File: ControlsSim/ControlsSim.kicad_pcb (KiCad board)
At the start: 2 copper layers, 100 x 100 mm, 25 parts, among them J2 Accelerator Pot, J3 Brake Button, J5 Motor Contactors, J6 Array Contactors, J7 Rotary Switch, SW2 SW_Rotary2x6

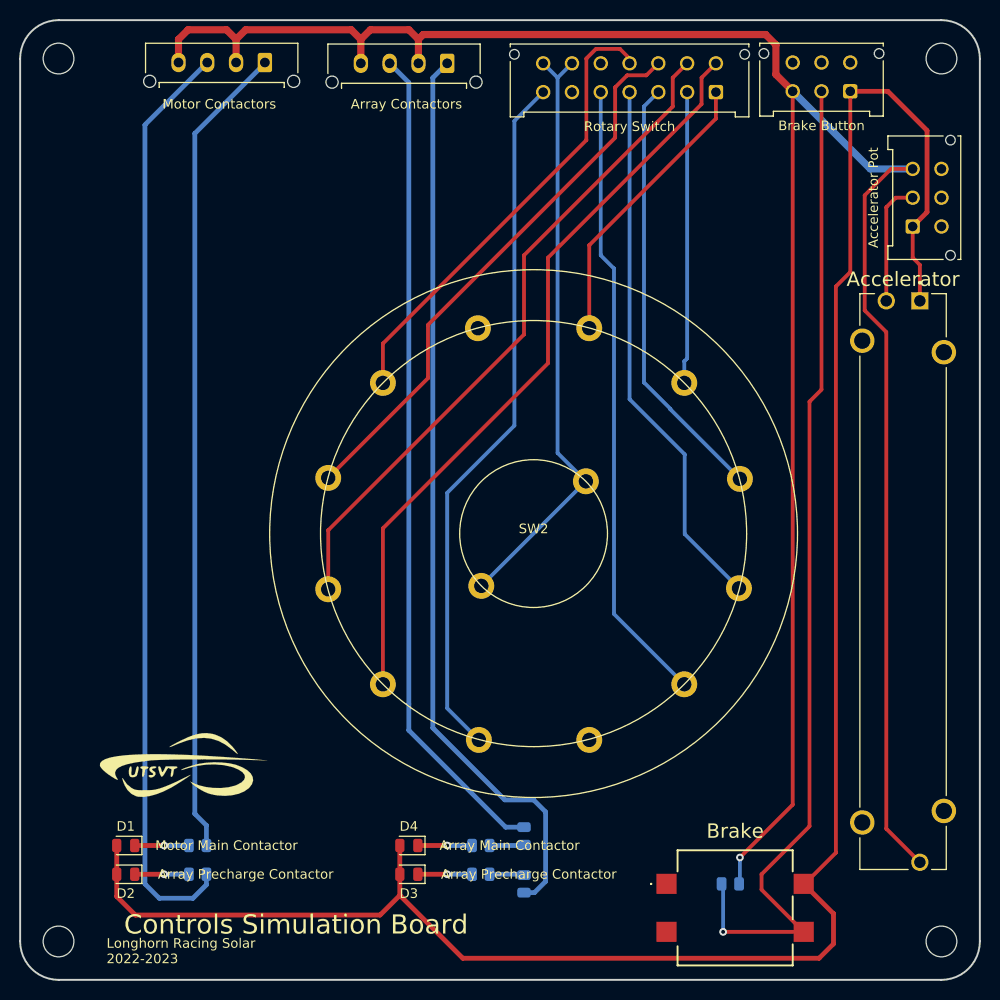
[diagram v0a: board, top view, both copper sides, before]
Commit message: shortened traces of contactor LEDs, moved upward
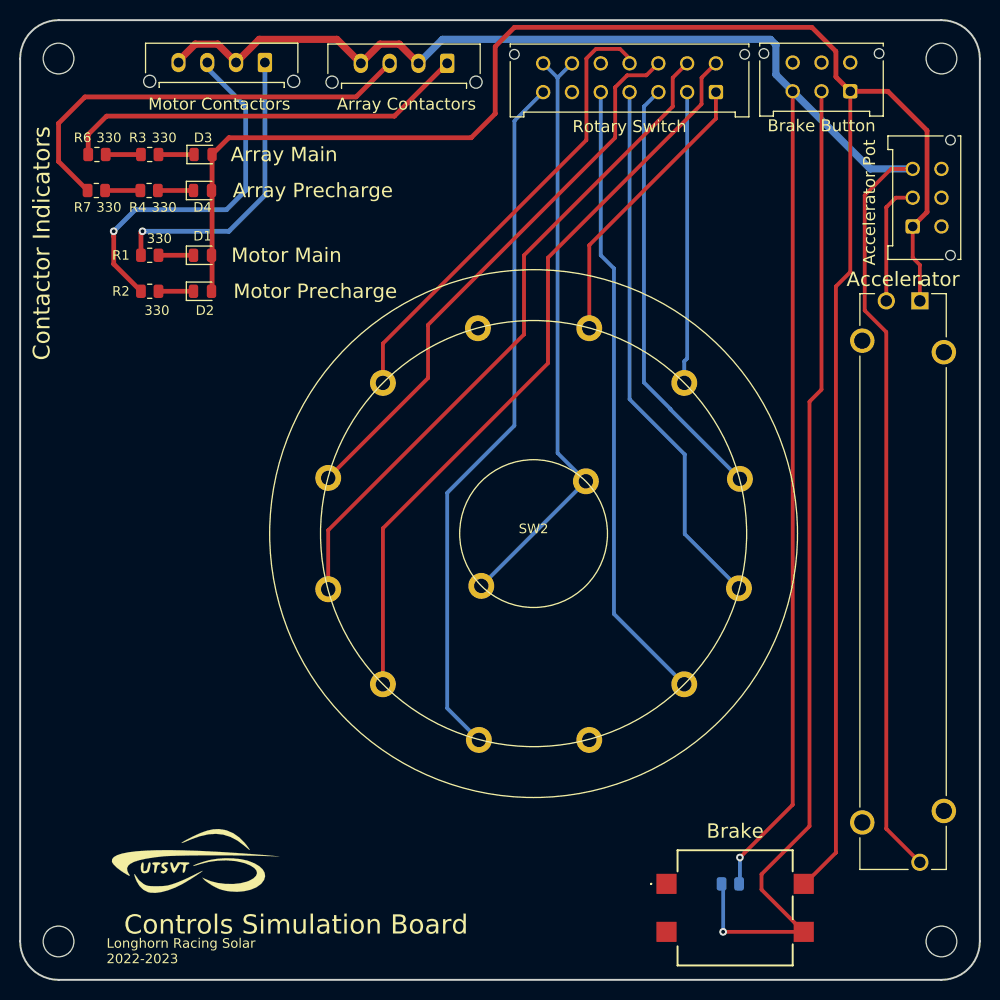
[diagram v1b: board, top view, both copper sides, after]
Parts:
- R1, R2, R3, R4, R6, R7: moved to F.Cu
- moved R6 88.1 mm to (108.0, 64.0), turned to 180 degrees
- moved R3 82.6 mm to (113.5, 64.0), turned to 180 degrees
- moved R7 80.7 mm to (107.9, 67.8), turned to 180 degrees
- moved D3 78.0 mm to (119.1, 64.0), turned to 0 degrees
- moved R4 76.5 mm to (113.4, 67.8), turned to 180 degrees
- moved D4 71.6 mm to (119.0, 67.8), turned to 0 degrees
- moved D1 62.0 mm to (119.0, 74.5), turned to 0 degrees
- moved R1 61.7 mm to (113.5, 74.5), turned to 180 degrees
- moved D2 61.3 mm to (119.0, 78.2), turned to 0 degrees
- moved R2 61.0 mm to (113.5, 78.2), turned to 0 degrees
- moved LOGO2 10.1 mm to (118.0, 137.8)
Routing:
- net /M_D_Pre2: track 97.0 -> 37.9 mm, vias 0 -> 1
- net /M_D_Mn2: track 85.1 -> 30.7 mm, vias 0 -> 1
- net /A_D_Mn2: track 95.2 -> 42.6 mm
- net /A_D_Pre2: track 86.5 -> 45.3 mm
- net GND: track 259.6 -> 253.2 mm
- net +3V3: track 210.7 -> 207.7 mm
- net /M_D_Pre1: track 5.65 -> 3.65 mm, vias 1 -> 0
- net /M_D_Mn1: track 5.65 -> 3.65 mm, vias 1 -> 0
- net /A_D_Pre1: track 5.65 -> 3.71 mm, vias 1 -> 0
- net /A_D_Mn1: track 5.65 -> 3.71 mm, vias 1 -> 0
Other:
- board text added: "Array Main"
- board text added: "Array Precharge"
- board text added: "Contactor Indicators"
- board text added: "Motor Main"
- board text added: "Motor Precharge"
- board text removed: "Array Main Contactor"
- board text removed: "Array Precharge Contactor"
- board text removed: "Motor Main Contactor"

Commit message: Changed LED colors to use all four colors, one for each contactor
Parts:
- added R1: 330, Resistor_SMD:R_0805_2012Metric, F.Cu at (113.5, 74.5)
- moved R3 14.2 mm to (113.5, 78.2), turned to 0 degrees
- moved R2 5.75 mm to (107.8, 74.5)
- moved R4 5.75 mm to (107.8, 78.2)
- moved R5 5.50 mm to (113.5, 64.0)
- renumbered R1 to R2, R2 to R4, R6 to R5, R4 to R6, R5 to R8
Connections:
- J5 pad 1: /M_D_Mn2 -> /M_D_Mn3
- J5 pad 3: /M_D_Pre2 -> /M_D_Pre3
- J6 pad 3: /A_D_Pre2 -> /A_D_Pre3
- R2 pad 1: /M_D_Mn1 -> /M_D_Mn2
- R2 pad 2: /M_D_Mn2 -> /M_D_Mn3
- R3 pad 1: /A_D_Mn1 -> /M_D_Pre2
- R3 pad 2: /X1 -> /M_D_Pre1
- R4 pad 1: /M_D_Pre2 -> /M_D_Pre3
- R4 pad 2: /M_D_Pre1 -> /M_D_Pre2
- R5 pad 1: /X1 -> /A_D_Mn1
- R6 pad 2: /X2 -> /A_D_Pre2
- R7 pad 1: /X2 -> /A_D_Pre2
- R7 pad 2: /A_D_Pre2 -> /A_D_Pre3
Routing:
- net /A_D_Pre3: track 0.00 -> 45.3 mm
- net /M_D_Pre3: track 0.00 -> 43.8 mm, vias 0 -> 1
- net /A_D_Pre2: track 45.3 -> 3.68 mm
- net /M_D_Mn3: track 0.00 -> 35.9 mm, vias 0 -> 1
- net /M_D_Pre2: track 37.9 -> 3.93 mm, vias 1 -> 0
- net /M_D_Mn2: track 30.7 -> 3.93 mm, vias 1 -> 0
- net /A_D_Mn2: track 42.6 -> 37.2 mm
- net /X2: track 3.68 -> 0.00 mm
- net /X1: track 3.68 -> 0.00 mm
